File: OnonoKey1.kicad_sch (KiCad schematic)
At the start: 85 parts, among them SW00 Switch, SW01 Switch, SW02 Switch, SW03 Switch, SW04 Switch, SW05 Switch, SW06 Switch, SW10 Switch, SW11 Switch, SW12 Switch, SW13 Switch, SW14 Switch, SW15 Switch, SW16 Switch, SW20 Switch, SW21 Switch, SW22 Switch, SW23 Switch, SW24 Switch, SW25 Switch, SW26 Switch, SW30 Switch, SW31 Switch, SW32 Switch, SW33 Switch, SW34 Switch, SW35 Switch, SW36 Switch, SW40 Switch, SW41 Switch, SW42 Switch, SW43 Switch, SW44 Switch, SW45 Switch, SW46 Switch, SW50 Switch, SW51 Switch, SW52 Switch, SW53 Switch, SW54 Switch, SW55 Switch, SW56 Switch, U1 RP2040_Zero

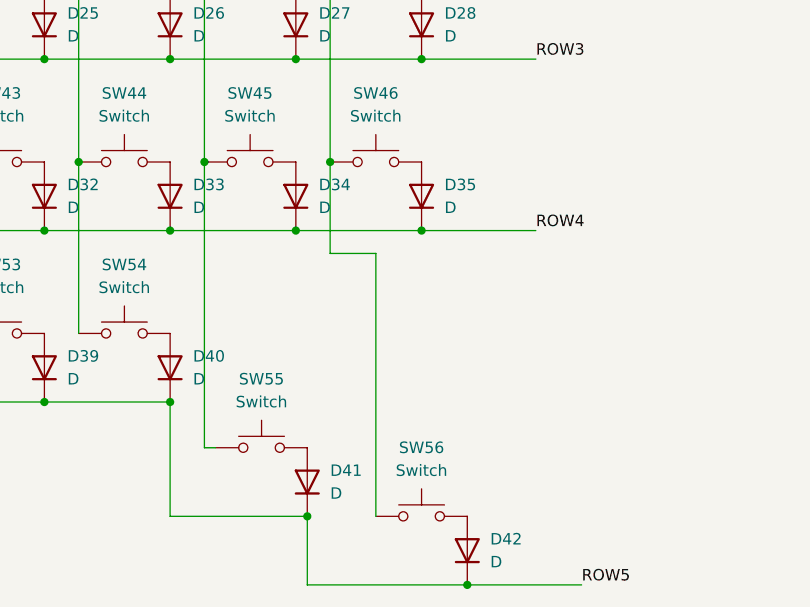
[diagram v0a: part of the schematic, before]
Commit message: Changed footprints, rearranged keys on pcb
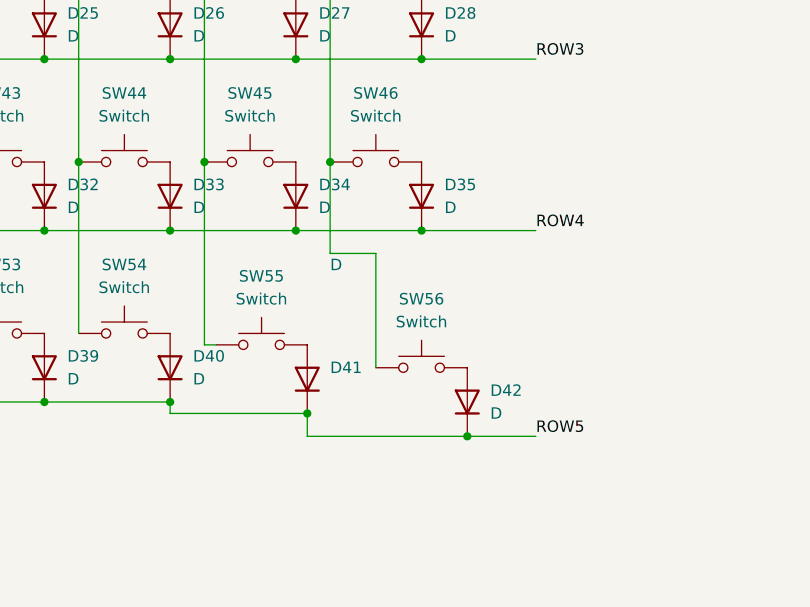
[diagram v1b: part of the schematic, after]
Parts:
- SW00, SW01, SW02, SW03, SW04, SW05, SW06, SW10, SW11, SW12, SW13, SW14, SW15, SW16, SW20, SW21, SW22, SW23, SW24, SW25, SW26, SW30, SW31, SW32, SW33, SW34, SW35, SW36, SW40, SW41, SW42, SW43, SW44, SW45, SW46, SW50, SW51, SW52, SW53, SW54, SW55, SW56: footprint ScottoKeebs_MX:MX_PCB_1.00u -> Daprice_Keyswitches:Kailh_socket_MX_optional_reversible_1u
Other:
- moved on the sheet: D41, D42, SW55, SW56

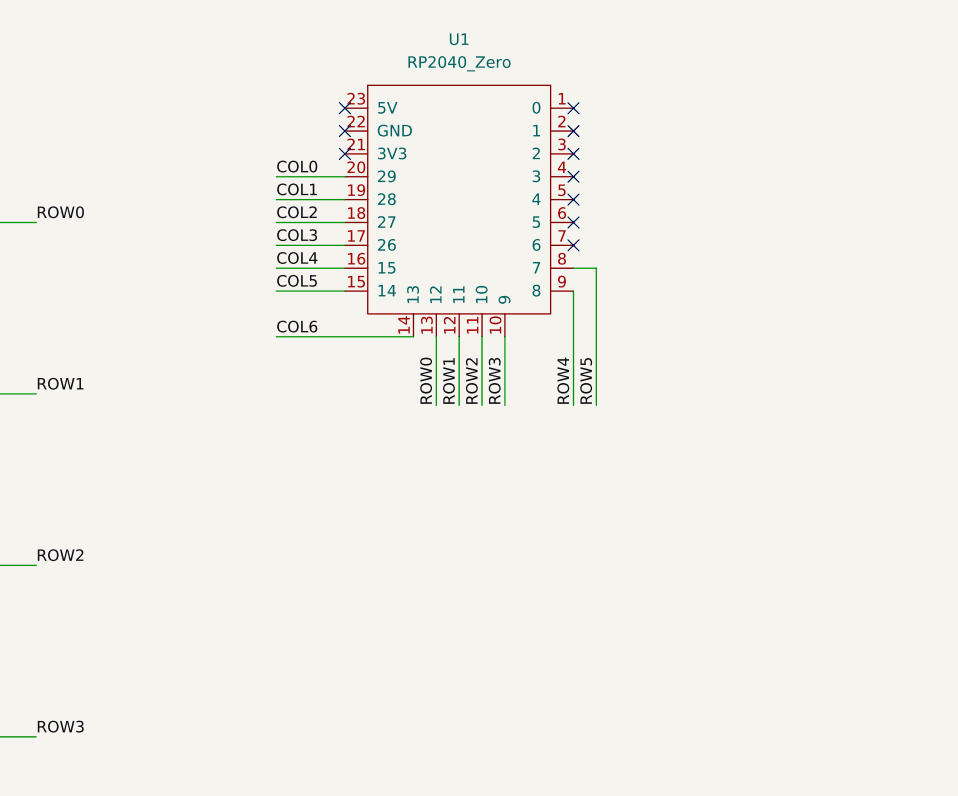
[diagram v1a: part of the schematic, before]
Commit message: Added M2 holes and two TRRS jacks for front and back
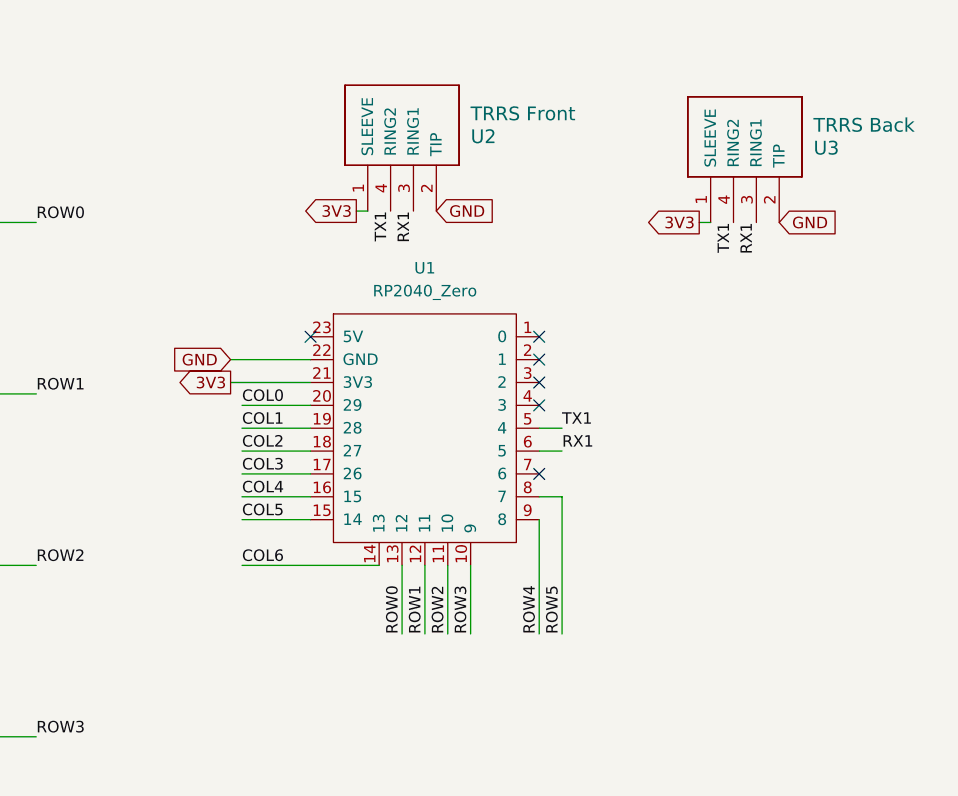
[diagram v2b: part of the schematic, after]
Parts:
- added U2: TRRS Front, ScottoKeebs_Components:TRRS_PJ-320A, symbol Scotto:Placeholder_TRRS
- added U3: TRRS Back, ScottoKeebs_Components:TRRS_PJ-320A, symbol Scotto:Placeholder_TRRS
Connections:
- net 3V3: now reaches U1.21 (3V3)
- net 3V3: now also U2.1 (SLEEVE), U3.1 (SLEEVE)
- net GND: now reaches U1.22 (GND)
- net GND: now also U2.2 (TIP), U3.2 (TIP)
- net TX1: now reaches U1.5 (4)
- net TX1: now also U2.4 (RING2), U3.4 (RING2)
- net RX1: now reaches U1.6 (5)
- net RX1: now also U2.3 (RING1), U3.3 (RING1)
- no-connect marks 10 -> 6
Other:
- moved on the sheet: U1

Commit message: some messing around without any result
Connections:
- net 3V3: now also U2.2 (TIP), U3.2 (TIP); no longer U2.1 (SLEEVE), U3.1 (SLEEVE)
- net GND: now also U2.1 (SLEEVE), U3.1 (SLEEVE); no longer U2.2 (TIP), U3.2 (TIP)
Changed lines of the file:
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@@
 		)
 	)
-	(global_label "GND"
-		(shape input)
+	(global_label "3V3"
+		(shape output)
 		(at 172.72 39.37 0)
 		(fields_autoplaced yes)
@@
 		)
 		(property "Intersheetrefs" "${INTERSHEET_REFS}"
-			(at 179.5757 39.37 0)
+			(at 179.2128 39.37 0)
 			(effects
 				(font
@@
 		)
 	)
-	(global_label "3V3"
-		(shape output)
-		(at 201.93 40.64 180)
+	(global_label "GND"
+		(shape input)
+		(at 163.83 39.37 180)
 		(fields_autoplaced yes)
 		(effects
@@
 		)
 		(property "Intersheetrefs" "${INTERSHEET_REFS}"
-			(at 195.4372 40.64 0)
+			(at 156.9743 39.37 0)
 			(effects
 				(font
@@
 				)
 				(justify right)
+				(hide yes)
+			)
+		)
+	)
+	(global_label "3V3"
+		(shape output)
+		(at 210.82 40.64 0)
+		(fields_autoplaced yes)
+		(effects
+			(font
+				(size 1.27 1.27)
+			)
+			(justify left)
+		)
+		(property "Intersheetrefs" "${INTERSHEET_REFS}"
+			(at 217.3128 40.64 0)
+			(effects
+				(font
+					(size 1.27 1.27)
+				)
+				(justify left)
 				(hide yes)
 			)
@@
 		)
 	)
-	(global_label "3V3"
-		(shape output)
-		(at 163.83 39.37 180)
+	(global_label "GND"
+		(shape input)
+		(at 201.93 40.64 180)
 		(fields_autoplaced yes)
 		(effects
@@
 		)
 		(property "Intersheetrefs" "${INTERSHEET_REFS}"
-			(at 157.3372 39.37 0)
+			(at 195.0743 40.64 0)
 			(effects
 				(font
@@
 				(hide yes)
 			)
-		)
-	)
-	(global_label "GND"
-		(shape input)
-		(at 210.82 40.64 0)
-		(fields_autoplaced yes)
-		(effects
-			(font
-				(size 1.27 1.27)
-			)
-			(justify left)
-		)
-		(property "Intersheetrefs" "${INTERSHEET_REFS}"
-			(at 217.6757 40.64 0)
-			(effects
-				(font
-					(size 1.27 1.27)
-				)
-				(justify left)
-				(hide yes)
-			)

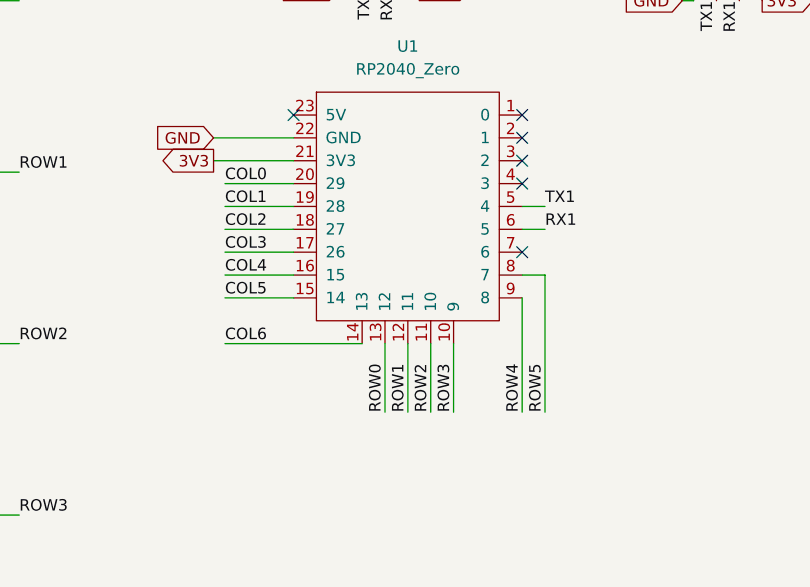
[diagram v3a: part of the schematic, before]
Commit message: Rearranging board outline, finishing optimising pins for routing, moving upper trrs jack down a little, connecting everything, making DRC errorless
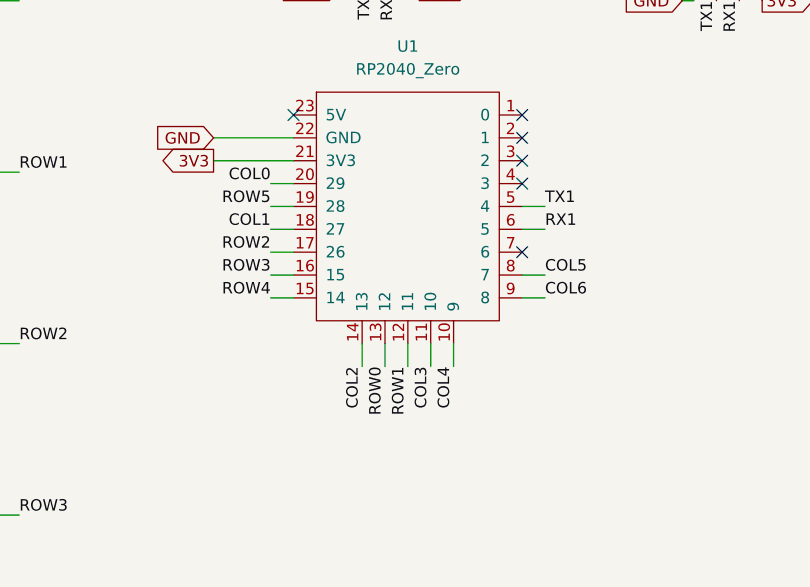
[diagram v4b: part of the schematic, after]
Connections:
- net COL1: now also U1.18 (27); no longer U1.19 (28)
- net COL2: now also U1.14 (13); no longer U1.18 (27)
- net COL3: now also U1.11 (10); no longer U1.17 (26)
- net COL4: now also U1.10 (9); no longer U1.16 (15)
- net COL5: now also U1.8 (7); no longer U1.15 (14)
- net COL6: now also U1.9 (8); no longer U1.14 (13)
- net ROW2: now also U1.17 (26); no longer U1.11 (10)
- net ROW3: now also U1.16 (15); no longer U1.10 (9)
- net ROW4: now also U1.15 (14); no longer U1.9 (8)
- net ROW5: now also U1.19 (28); no longer U1.8 (7)
